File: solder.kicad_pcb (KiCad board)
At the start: 2 copper layers, 41 x 36.6 mm, 6 parts

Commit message: update!!! made LEDs blink
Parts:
- added C1: C, Capacitor_THT:CP_Radial_D8.0mm_P5.00mm, F.Cu at (114.4, 143.0)
- added C2: C, Capacitor_THT:CP_Radial_D8.0mm_P5.00mm, F.Cu at (140.4, 143.0)
- added Q1: NPN, Package_TO_SOT_THT:TO-92L_HandSolder, F.Cu at (140.0, 131.5)
- added Q2: NPN, Package_TO_SOT_THT:TO-92L_HandSolder, F.Cu at (110.0, 134.0)
- added R3: R, Resistor_THT:R_Axial_DIN0207_L6.3mm_D2.5mm_P7.62mm_Horizontal, F.Cu at (140.0, 120.0)
- added R4: R, Resistor_THT:R_Axial_DIN0207_L6.3mm_D2.5mm_P7.62mm_Horizontal, F.Cu at (144.0, 120.0)
- moved BT1 61.5 mm to (125.0, 125.0)
- moved G*** 54.2 mm to (110.0, 107.0)
- moved D1 45.3 mm to (115.0, 114.0)
- moved D2 40.7 mm to (135.0, 114.0)
- moved R1 40.6 mm to (106.0, 120.0), turned to -90 degrees
- moved R2 38.0 mm to (110.0, 120.0), turned to -90 degrees
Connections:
- R1 pad 1: Net-(D1-K) -> Net-(BT1-+)
- R1 pad 2: Net-(BT1--) -> Net-(D1-K)
- R2 pad 1: Net-(D2-K) -> Net-(BT1-+)
- R2 pad 2: Net-(BT1--) -> Net-(Q2-B)
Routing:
- net Net-(BT1--): track 30.0 -> 0.00 mm
- net Net-(BT1-+): track 18.1 -> 0.00 mm
- net Net-(D1-K): track 6.62 -> 0.00 mm
- net Net-(D2-K): track 6.24 -> 0.00 mm
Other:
- board size 41 x 36.6 mm -> 48 x 49.1 mm
- board text removed: "*meow*"

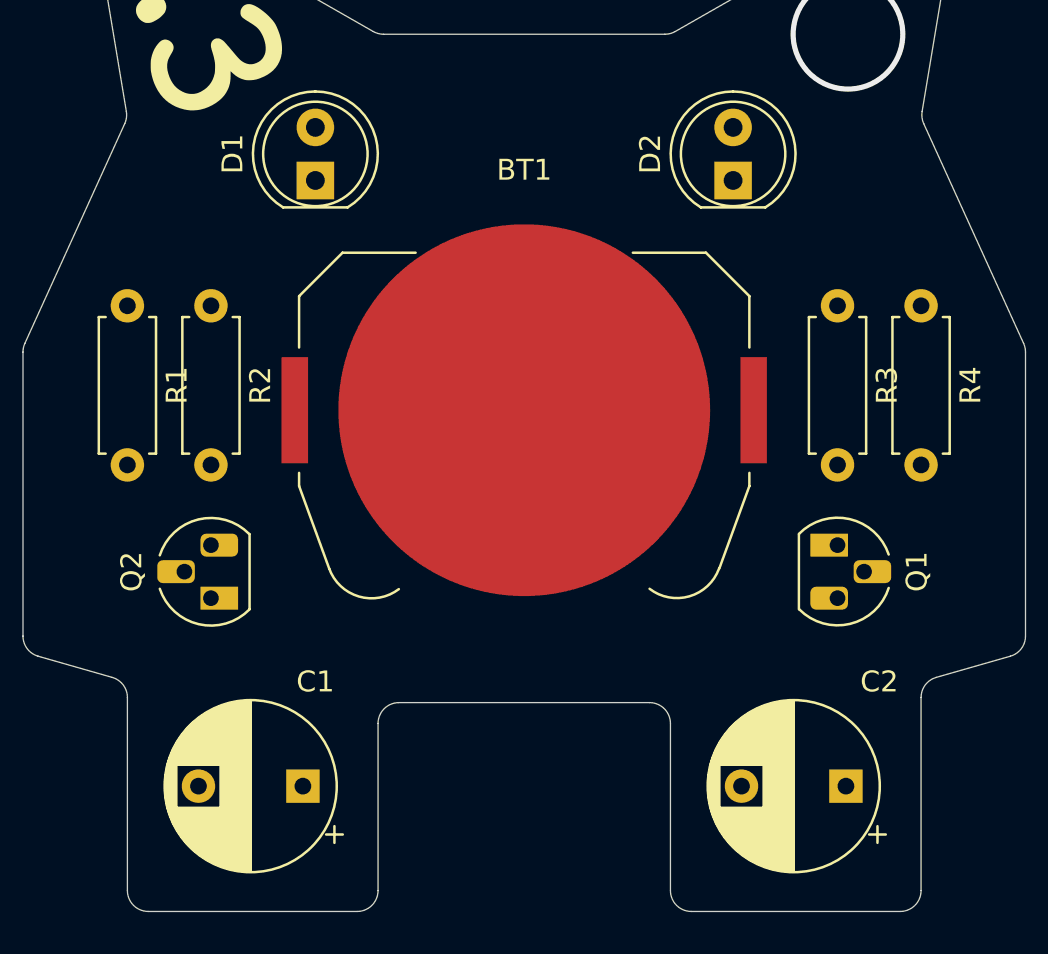
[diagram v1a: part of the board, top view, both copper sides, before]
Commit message: added pcb traces and back silkscreen
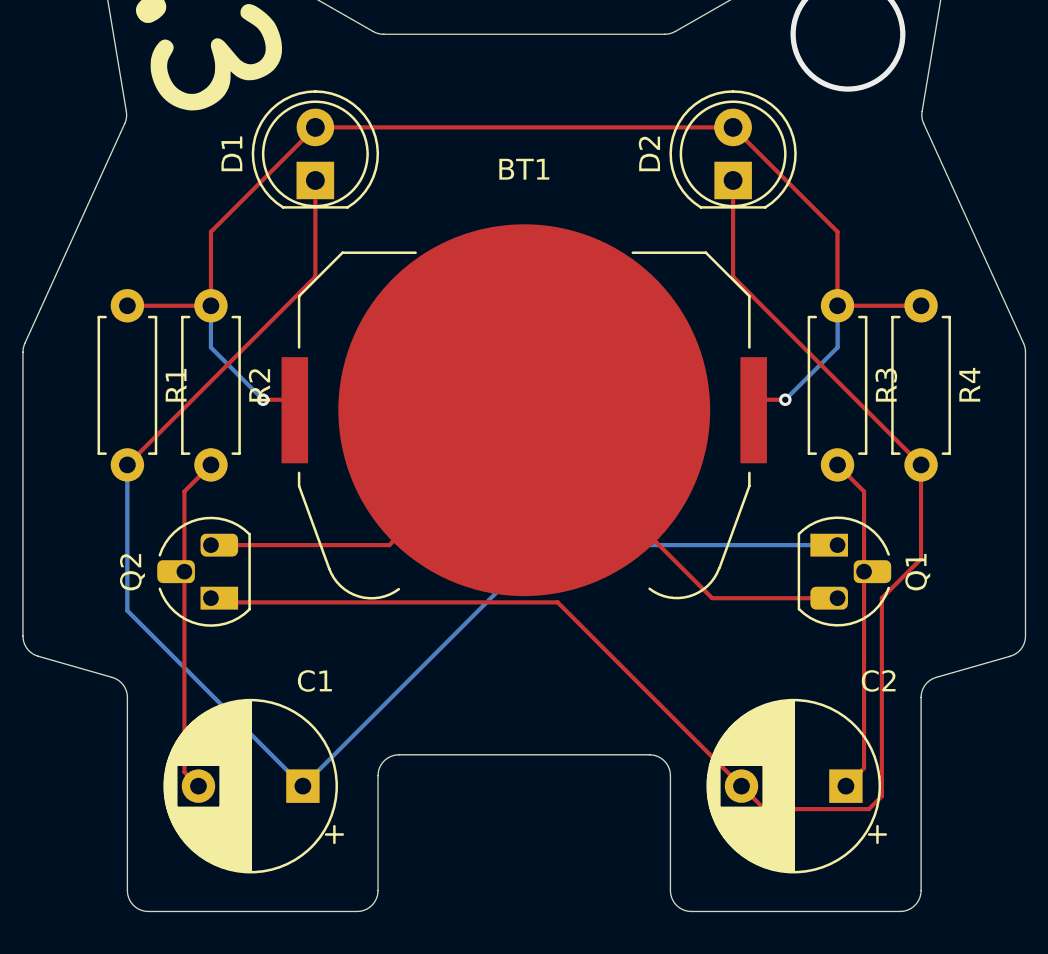
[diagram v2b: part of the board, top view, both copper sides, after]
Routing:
- net Net-(D2-K): track 0.00 -> 70.6 mm
- net Net-(D1-K): track 0.00 -> 66.6 mm
- net Net-(BT1-+): track 0.00 -> 63.7 mm, vias 0 -> 2
- net Net-(BT1--): track 0.00 -> 36.4 mm
- net Net-(Q1-B): track 0.00 -> 16.3 mm
- net Net-(Q2-B): track 0.00 -> 16.2 mm
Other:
- outline, holes or cut-outs redrawn
- board text added: "built for solder"
- board text added: "meow!"
